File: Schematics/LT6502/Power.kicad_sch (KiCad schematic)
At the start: 85 parts, among them IC2 MP2636GR-P, J2 USBPD_PROG, J3 USB_C_Receptacle_USB2.0_16P, J4 BATTERY JST PH-2A, Q1 STL9P3LLH6, Q3 STL9P3LLH6, U6 STUSB4500QTR, U7 AP63203WU

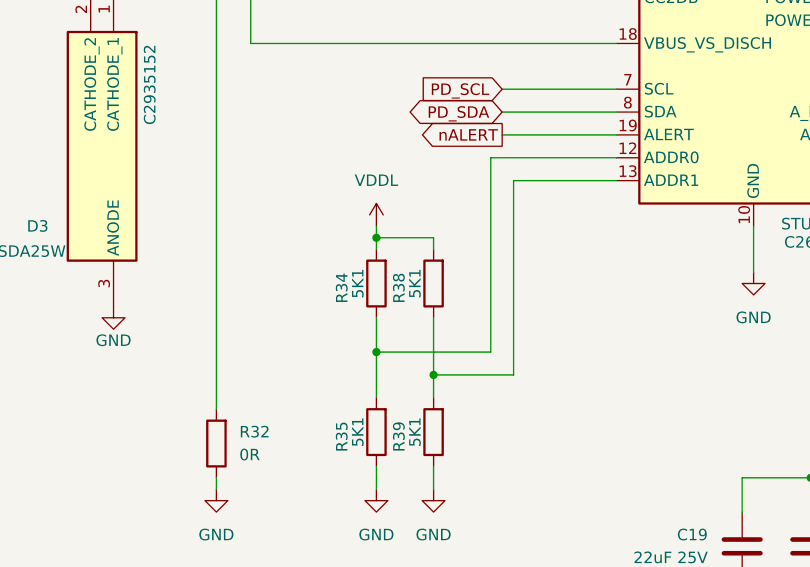
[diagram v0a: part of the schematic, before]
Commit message: Tweaks to Schematics
Shrunk main PCB
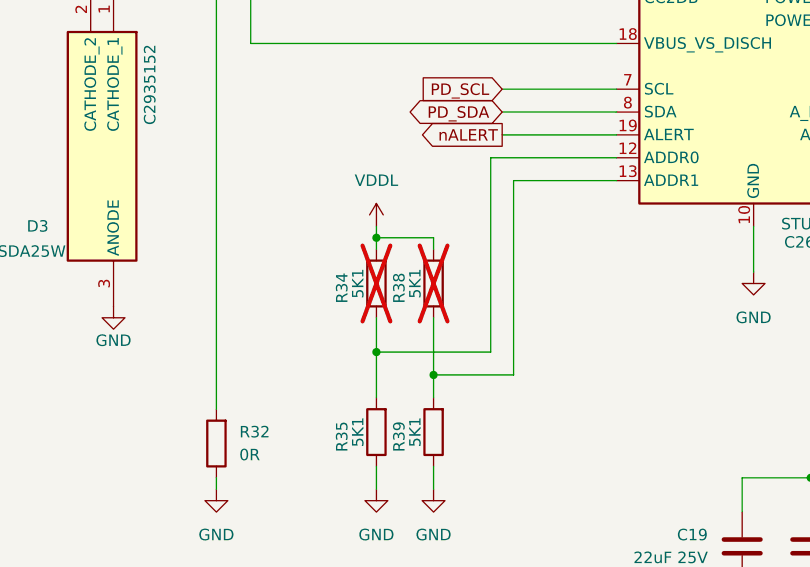
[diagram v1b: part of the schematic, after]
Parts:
- R34, R38: now not fitted
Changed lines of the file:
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@@
 		(in_bom yes)
 		(on_board yes)
-		(dnp no)
+		(dnp yes)
 		(property "Reference" "R34"
 			(at 119.38 112.268 90)
@@
 		(in_bom yes)
 		(on_board yes)
-		(dnp no)
+		(dnp yes)
 		(property "Reference" "R38"
 			(at 125.73 112.268 90)

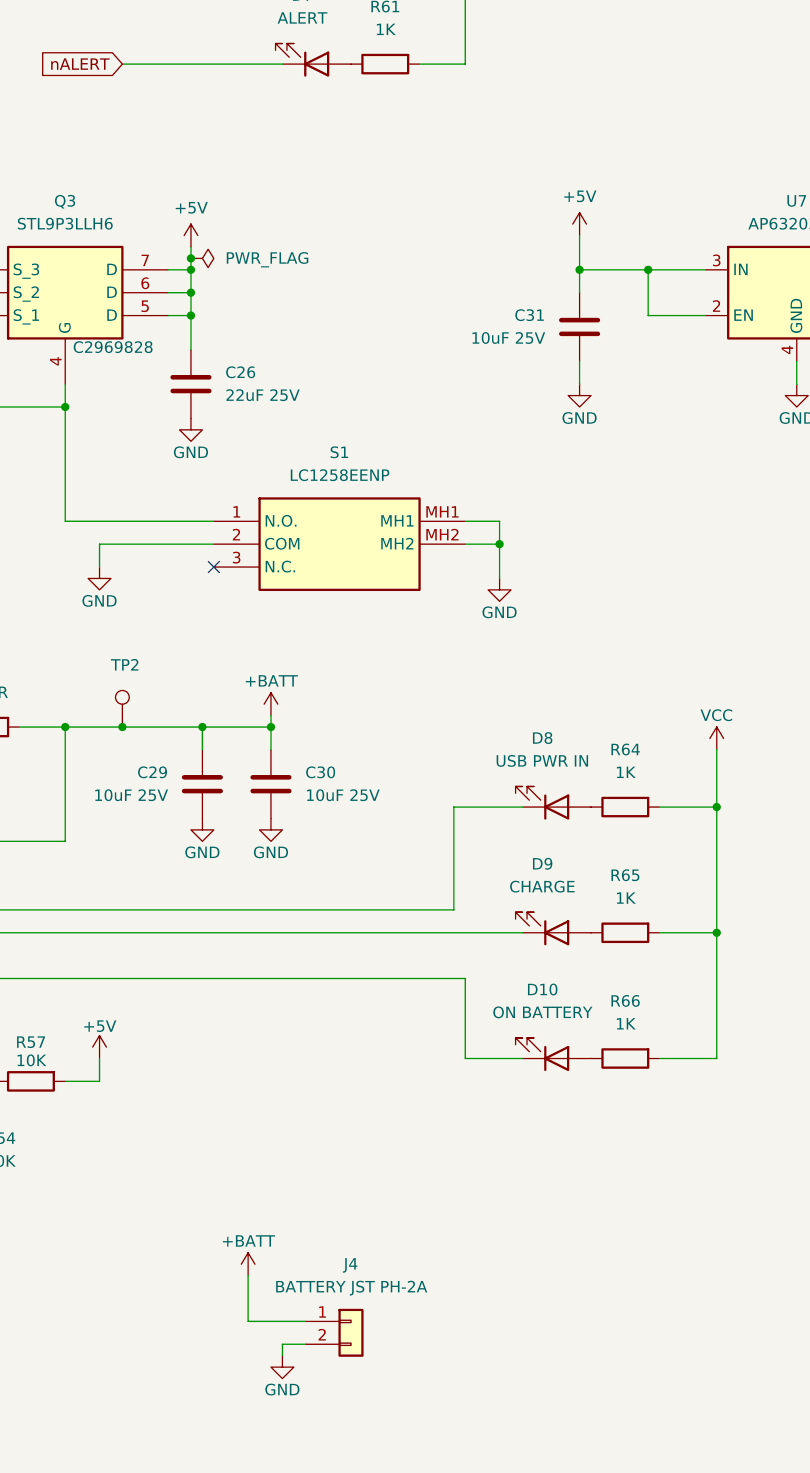
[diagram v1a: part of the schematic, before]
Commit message: Further work on Schematics, All parts placed on PCB
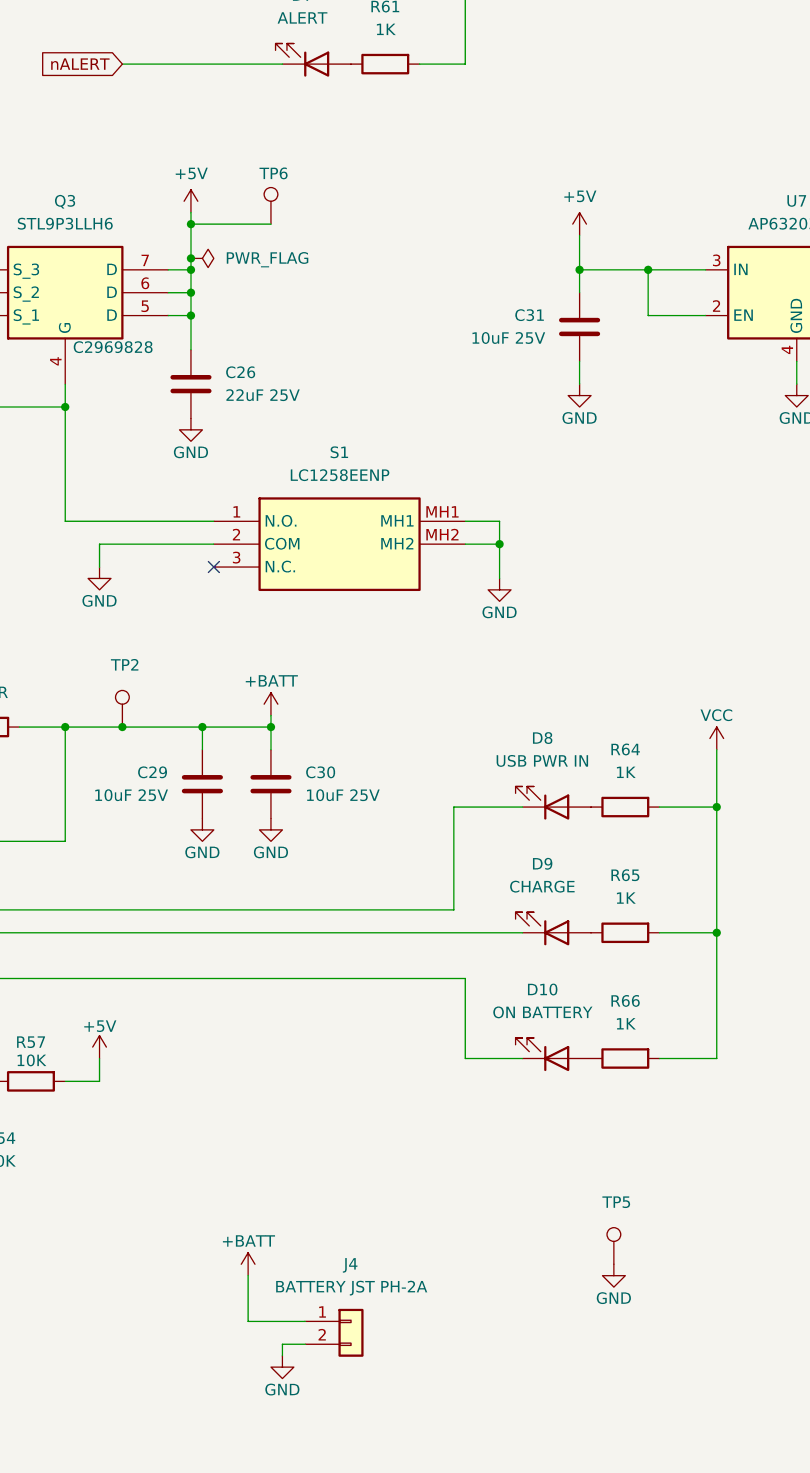
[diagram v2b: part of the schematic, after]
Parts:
- added TP5, TP6: TestPoint, TestPoint:TestPoint_Loop_D1.80mm_Drill1.0mm_Beaded, symbol Connector:TestPoint
- R36, R37, R40, R41, R42, R43, R44, R45, R46, R47, R48, R49, R51, R52, R54, R57, R59, R60, R61, R64, R65, R66, R84: footprint Resistor_SMD:R_0603_1608Metric_Pad0.98x0.95mm_HandSolder -> Resistor_SMD:R_0402_1005Metric
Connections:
- net +5V: now also TP6.1
- net GND: now also TP5.1

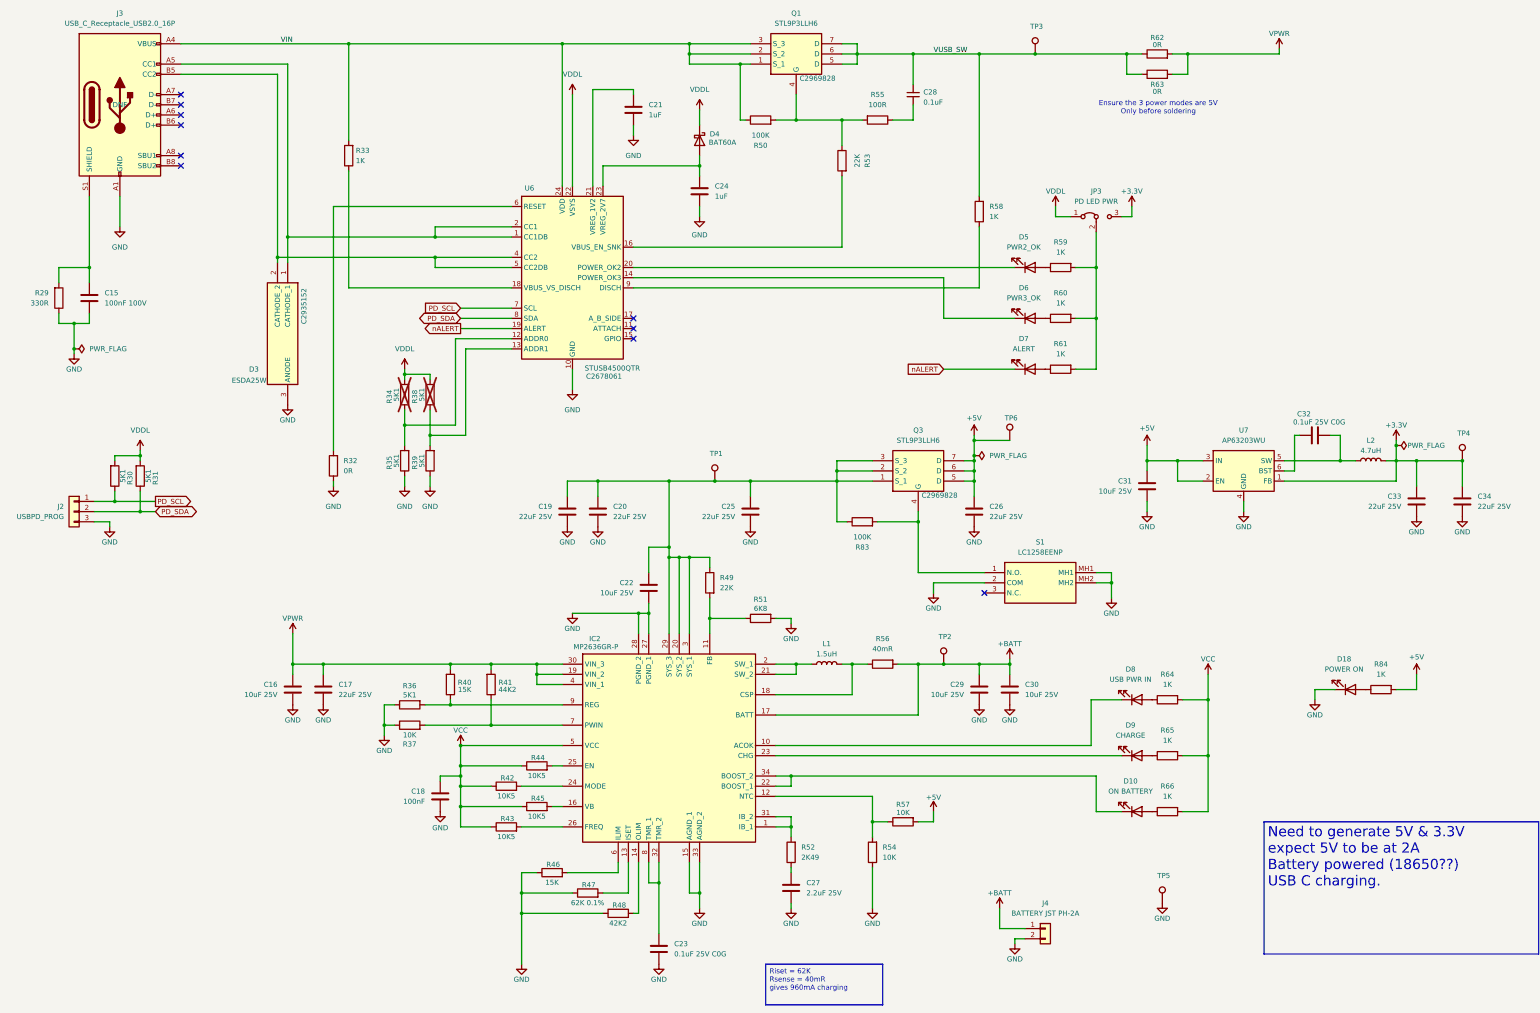
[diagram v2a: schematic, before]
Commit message: Updated BoMs ordered PCBs
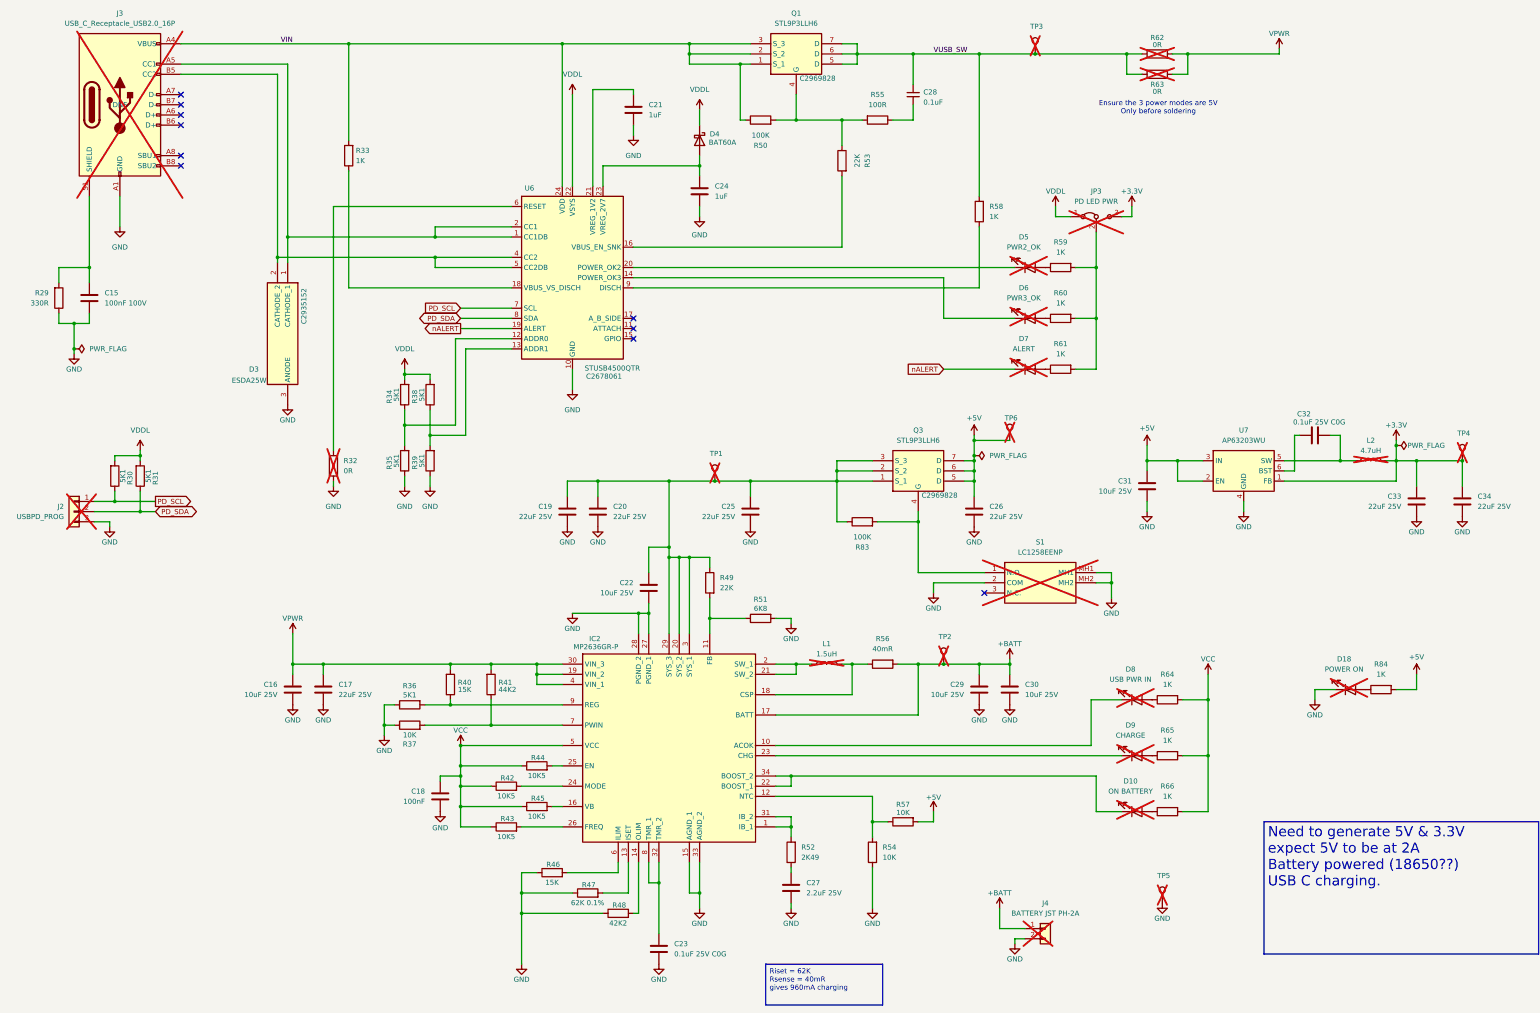
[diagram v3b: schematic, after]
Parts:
- C15, C28: LCSC C14663 -> C113803
- C16, C22, C29, C30, C31: LCSC (none) -> C15850
- C17, C19, C20, C25, C26, C33, C34: LCSC (none) -> C45783
- C18: LCSC C49678 -> C113803
- C23, C32: LCSC C49678 -> C91183
- C27: LCSC (none) -> C19110
- D10, D18, D5, D6, D7, D8, D9, J2, J4, JP3, L1, L2: LCSC (none) -> DNF; now not fitted
- IC2: LCSC (none) -> C128212
- J3, R32, R62, R63, S1, TP1, TP2, TP3, TP4, TP5, TP6: now not fitted
- R29: LCSC DNF -> C25104
- R33, R58: LCSC DNF -> C11702
- R34, R38: now fitted
- R36: LCSC C23179 -> C25905
- R37, R54, R57: LCSC C23179 -> C25744
- R40, R46: LCSC C23179 -> C25756
- R41, R48: LCSC C23179 -> C11565
- R42, R43, R44, R45: LCSC C23179 -> C25850
- R47: LCSC C23179 -> C852874
- R49: LCSC C23179 -> C25768
- R50, R83: LCSC DNF -> C25741
- R51: LCSC C23179 -> C25917
- R52: LCSC C23179 -> C2692737
- R53: LCSC DNF -> C25768
- R55: LCSC DNF -> C25076
- R56: LCSC C23179 -> C2774938
- R59, R60, R61, R64, R65, R66, R84: LCSC C23179 -> C11702
- U7: LCSC (none) -> C780769

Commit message: Auto stash before merge of "main" and "origin/main"
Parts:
- D10, D18, D8, D9, J2, J3, J4, L1, L2, S1: now fitted
- R34, R38: now not fitted
- R46: value 15K -> 51K; LCSC C25756 -> ???
- R47: value 62K 0.1% -> 120K; LCSC C852874 -> ???
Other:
- note added: "GREEN"
- note added: "ORANGE"
- note added: "RED"
- note added: "WHITE"
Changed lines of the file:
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@@
 		)
 	)
+	(text "ORANGE"
+		(exclude_from_sim no)
+		(at 306.07 218.948 0)
+		(effects
+			(font
+				(size 1.27 1.27)
+			)
+		)
+	)
+	(text "RED"
+		(exclude_from_sim no)
+		(at 305.816 204.978 0)
+		(effects
+			(font
+				(size 1.27 1.27)
+			)
+		)
+	)
+	(text "GREEN"
+		(exclude_from_sim no)
+		(at 359.918 189.23 0)
+		(effects
+			(font
+				(size 1.27 1.27)
+			)
+		)
+	)
+	(text "WHITE"
+		(exclude_from_sim no)
+		(at 305.816 191.008 0)
+		(effects
+			(font
+				(size 1.27 1.27)
+			)
+		)
+	)
+	(text_box "Rilim = 15K\ngives max charge current 3A!\n\nRilim = 51K\ngives max charge of 900mA\n\n"
+		(exclude_from_sim no)
+		(at 114.3 226.06 0)
+		(size 31.75 16.51)
+		(margins 0.9525 0.9525 0.9525 0.9525)
+		(stroke
+			(width 0)
+			(type solid)
+		)
+		(fill
+			(type none)
+		)
+		(effects
+			(font
+				(size 1.27 1.27)
+			)
+			(justify left top)
+		)
+	)
 	(text_box "Need to generate 5V & 3.3V\nexpect 5V to be at 2A\nBattery powered (18650??) \nUSB C charging."
 		(exclude_from_sim no)
@@
 		)
 	)
-	(text_box "Riset = 62K \nRsense = 40mR\ngives 960mA charging"
+	(text_box "Riset = 62K \nRsense = 40mR\ngives 960mA charging\n\nRiset = 120K\nRSense = 40mR\nGives 500mA charging"
+		(exclude_from_sim no)
+		(at 114.3 245.11 0)
+		(size 31.75 16.51)
+		(margins 0.9525 0.9525 0.9525 0.9525)
+		(stroke
+			(width 0)
+			(type solid)
+		)
+		(fill
+			(type none)
+		)
+		(effects
+			(font
+				(size 1.27 1.27)
+			)
+			(justify left top)
+		)
+	)
+	(text_box "Rolim = 42.2K\ngives sax output current 1.3A\n\nRolim = 22K\nGives max output current 2.5A"
 		(exclude_from_sim no)
-		(at 213.36 254 0)
-		(size 29.21 10.16)
+		(at 114.3 264.16 0)
+		(size 31.75 16.51)
 		(margins 0.9525 0.9525 0.9525 0.9525)
 		(stroke
@@
 		(in_bom yes)
 		(on_board yes)
-		(dnp yes)
+		(dnp no)
 		(fields_autoplaced yes)
 		(property "Reference" "D10"
@@
 		(in_bom yes)
 		(on_board yes)
-		(dnp yes)
+		(dnp no)
 		(property "Reference" "J4"
 			(at 283.21 238.76 0)
@@
 		(in_bom yes)
 		(on_board yes)
-		(dnp yes)
+		(dnp no)
 		(fields_autoplaced yes)
 		(property "Reference" "L1"
@@
 		(in_bom yes)
 		(on_board yes)
-		(dnp no)
+		(dnp yes)
 		(property "Reference" "R34"
 			(at 119.38 112.268 90)
@@
 		(in_bom yes)
 		(on_board yes)
-		(dnp yes)
+		(dnp no)
 		(fields_autoplaced yes)
 		(property "Reference" "D9"
@@
 			)
 		)
-		(property "Value" "15K"
+		(property "Value" "51K"
 			(at 159.9988 233.5961 90)
 			(effects
@@
 			)
 		)
-		(property "LCSC" "C25756"
+		(property "LCSC" "???"
 			(at 160.02 231.14 90)
 			(effects
@@
 		(in_bom yes)
 		(on_board yes)
-		(dnp yes)
+		(dnp no)
 		(fields_autoplaced yes)
 		(property "Reference" "D18"
@@
 			)
 		)
-		(property "Value" "62K 0.1%"
+		(property "Value" "120K"
 			(at 168.8888 238.6761 90)
 			(effects
@@
 			)
 		)
-		(property "LCSC" "C852874"
+		(property "LCSC" "???"
 			(at 168.91 236.22 90)
 			(effects
@@
 		(in_bom yes)
 		(on_board yes)
-		(dnp yes)
+		(dnp no)
 		(fields_autoplaced yes)
 		(property "Reference" "D8"
@@
 		(in_bom yes)
 		(on_board yes)
-		(dnp no)
+		(dnp yes)
 		(property "Reference" "R38"
 			(at 125.73 112.268 90)
@@
 		(in_bom yes)
 		(on_board yes)
-		(dnp yes)
+		(dnp no)
 		(property "Reference" "S1"
 			(at 281.94 148.59 0)
@@
 		(in_bom yes)
 		(on_board yes)
-		(dnp yes)
+		(dnp no)
 		(fields_autoplaced yes)
 		(property "Reference" "J3"
@@
 		(in_bom yes)
 		(on_board yes)
-		(dnp yes)
+		(dnp no)
 		(fields_autoplaced yes)
 		(property "Reference" "J2"
@@
 		(in_bom yes)
 		(on_board yes)
-		(dnp yes)
+		(dnp no)
 		(fields_autoplaced yes)
 		(property "Reference" "L2"

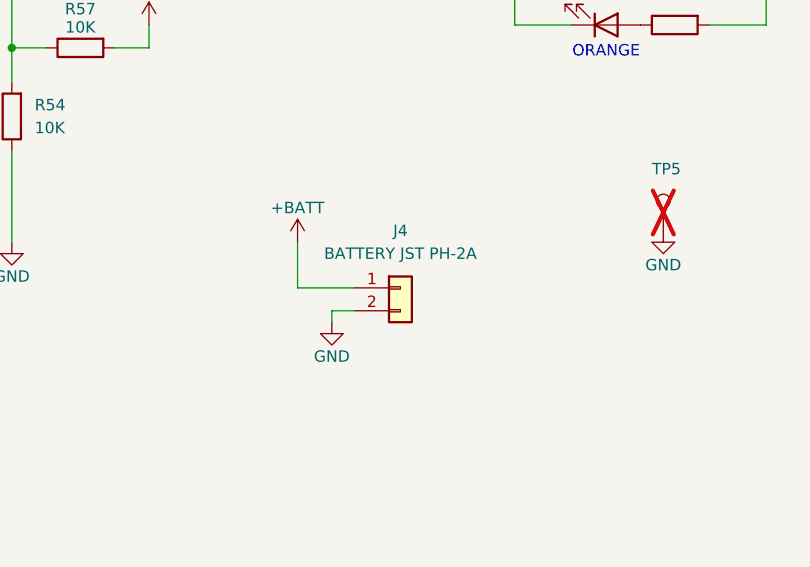
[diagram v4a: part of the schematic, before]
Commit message: Updated Schematic/PCB
Fixed battery connector polarity to save swapping wires.
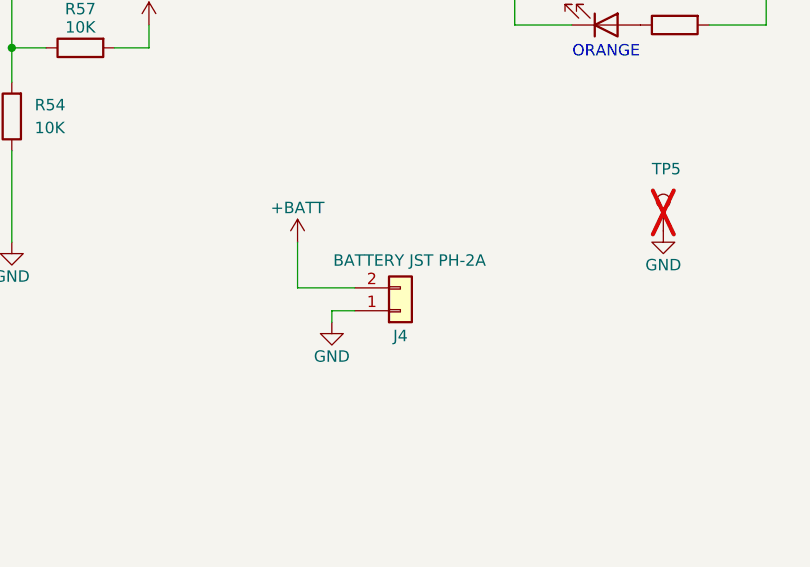
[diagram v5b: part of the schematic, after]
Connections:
- net +BATT: now also J4.2 (Pin_2); no longer J4.1 (Pin_1)
- net GND: now also J4.1 (Pin_1); no longer J4.2 (Pin_2)
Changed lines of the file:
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@@
 	(symbol
 		(lib_id "Connector_Generic:Conn_01x02")
-		(at 283.21 245.11 0)
+		(at 283.21 247.65 0)
+		(mirror x)
 		(unit 1)
 		(exclude_from_sim no)
@@
 		(dnp no)
 		(property "Reference" "J4"
-			(at 283.21 238.76 0)
+			(at 283.21 250.444 0)
 			(effects
 				(font
@@
 		)
 		(property "Value" "BATTERY JST PH-2A"
-			(at 283.21 241.3 0)
+			(at 284.226 242.062 0)
 			(effects
 				(font
@@
 		)
 		(property "Footprint" "S2B-XH-A_LF__SN_:SHDRRA2W80P0X250_1X2_740X1150X610P"
-			(at 283.21 245.11 0)
+			(at 283.21 247.65 0)
 			(effects
 				(font
@@
 		)
 		(property "Datasheet" "~"
-			(at 283.21 245.11 0)
+			(at 283.21 247.65 0)
 			(effects
 				(font
@@
 		)
 		(property "Description" "Generic connector, single row, 01x02, script generated (kicad-library-utils/schlib/autogen/connector/)"
-			(at 283.21 245.11 0)
+			(at 283.21 247.65 0)
 			(effects
 				(font
@@
 		)
 		(property "Mouser Part Number" "306-S2B-XH-ALFSN"
-			(at 283.21 245.11 0)
+			(at 283.21 247.65 0)
 			(effects
 				(font
@@
 		)
 		(property "LCSC" "DNF"
-			(at 283.21 245.11 0)
+			(at 283.21 247.65 0)
 			(effects
 				(font
